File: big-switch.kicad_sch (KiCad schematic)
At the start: 7 parts, among them J1 Conn_01x07_Socket, SW1 SW_Push, SW2 RotaryEncoder_Switch, SW3 RotaryEncoder_Switch, U1 ProMicro

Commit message: routing ocmplete
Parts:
- J1: symbol Connector:Conn_01x07_Socket -> Connector:Conn_01x08_Socket
- SW2, SW3: footprint (none) -> Keebio-Parts:RotaryEncoder_EC11B-Horizontal-Dual
- U1: value ProMicro -> LonganNano; symbol keebio:ProMicro -> ws2812b:Longan_Nano
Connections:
- net VCC is gone; now on net +3V3: J1.2 (Pin_2)
- net +3V3: now also U1.2 (3.3v)
- net +5V: now also U1.1 (5v)
- net AUDIO: now also U1.24 (A2)
- net DISP_BL: now also J1.8 (Pin_8), U1.20 (C14); no longer J1.7 (Pin_7)
- net DISP_CS: now also J1.7 (Pin_7), U1.21 (C13); no longer J1.6 (Pin_6)
- net DISP_DC: now also J1.6 (Pin_6), U1.22 (A0); no longer J1.5 (Pin_5)
- net ENC1_A: now also U1.5 (B14)
- net ENC1_B: now also U1.6 (B15)
- net ENC1_SW: now also U1.7 (A8)
- net ENC2_A: now also U1.8 (A11)
- net ENC2_B: now also U1.9 (A12)
- net ENC2_SW: now also U1.10 (B4)
- net GND: now also U1.16 (GND), U1.17 (GND)
- net GPIO_X1: now also U1.31 (B1)
- net GPIO_X2: now also U1.30 (B0)
- net MISO: now also U1.28 (A6)
- net MOSI: now also U1.29 (A7)
- net SCL: now also U1.12 (B6)
- net SCLK: now also U1.27 (A5)
- net SDA: now also U1.13 (B7)
- net SW_1: now also U1.3 (B12)
- net VIK_CS: now also U1.26 (A4)
- net VIK_RGB: now also U1.32 (B10)
- no-connect marks 0 -> 9

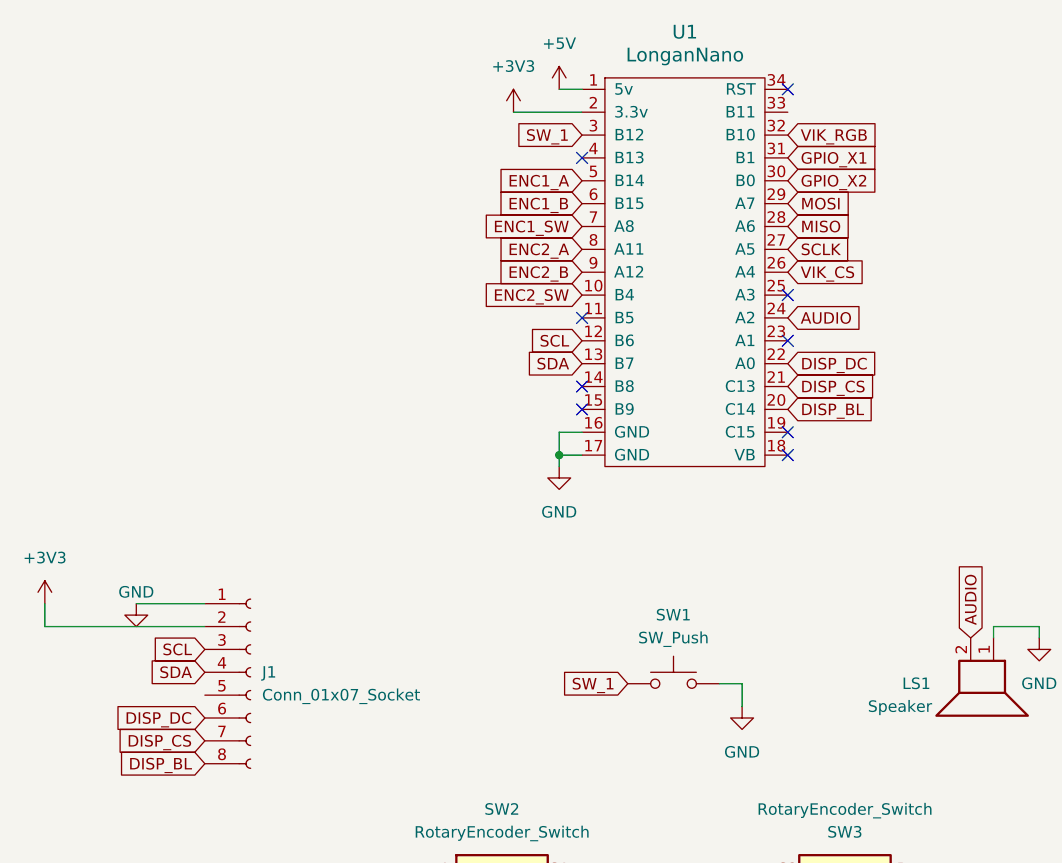
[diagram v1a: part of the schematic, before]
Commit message: flipped mcu side, rerouted
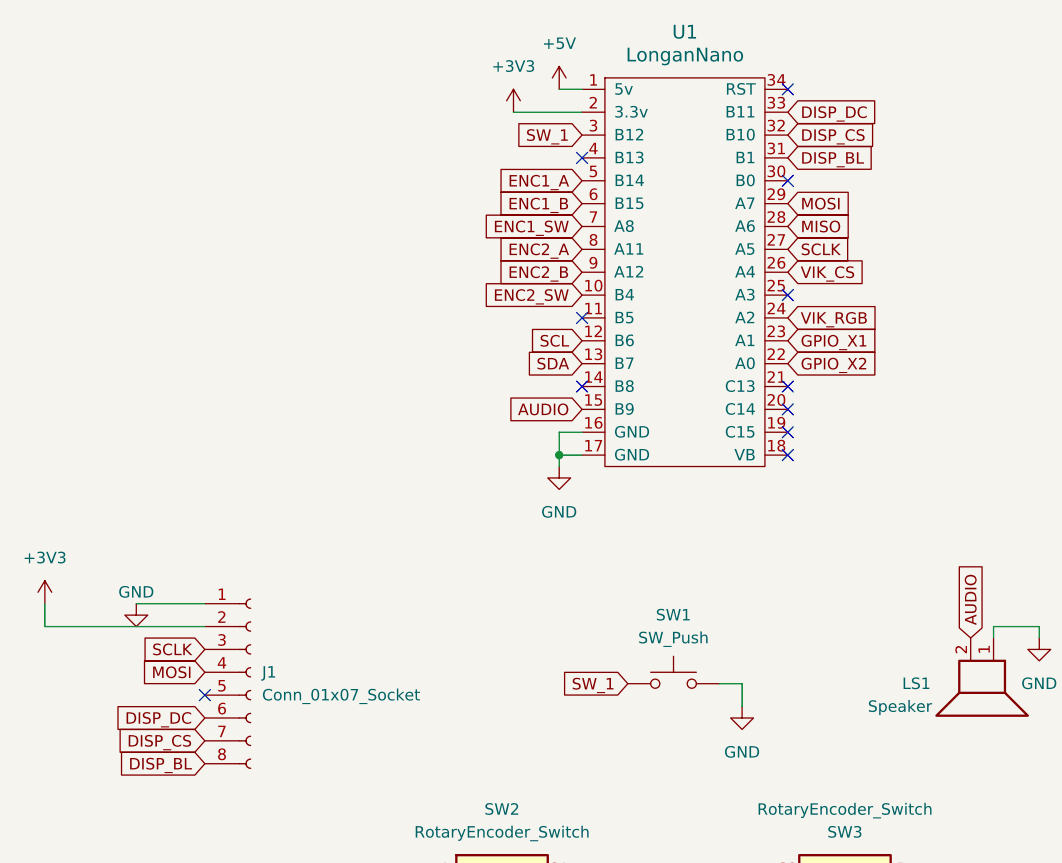
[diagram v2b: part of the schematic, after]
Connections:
- net AUDIO: now also U1.15 (B9); no longer U1.24 (A2)
- net DISP_BL: now also U1.31 (B1); no longer U1.20 (C14)
- net DISP_CS: now also U1.32 (B10); no longer U1.21 (C13)
- net DISP_DC: now also U1.33 (B11); no longer U1.22 (A0)
- net GPIO_X1: now also U1.23 (A1); no longer U1.31 (B1)
- net GPIO_X2: now also U1.22 (A0); no longer U1.30 (B0)
- net MOSI: now also J1.4 (Pin_4)
- net SCL: no longer J1.3 (Pin_3)
- net SCLK: now also J1.3 (Pin_3)
- net SDA: no longer J1.4 (Pin_4)
- net VIK_RGB: now also U1.24 (A2); no longer U1.32 (B10)
- no-connect marks 9 -> 11

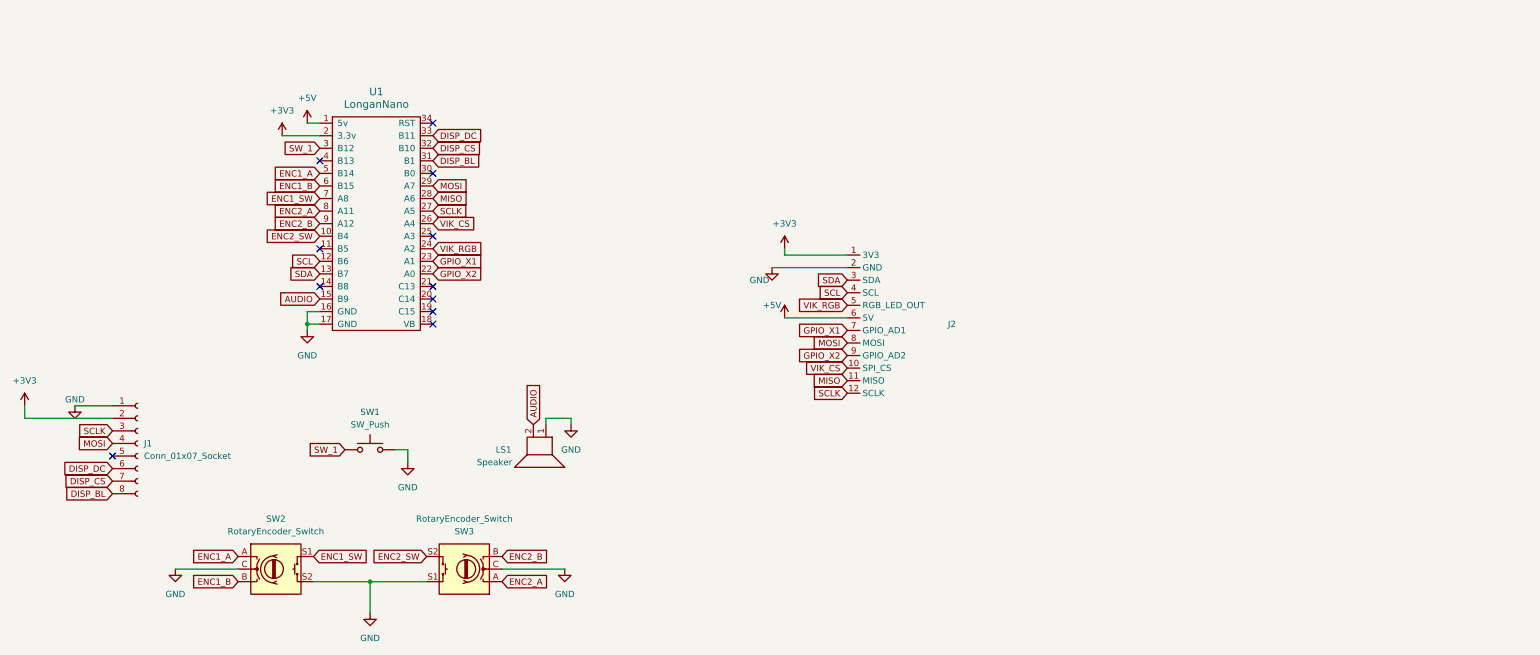
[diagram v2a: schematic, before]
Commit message: added LED
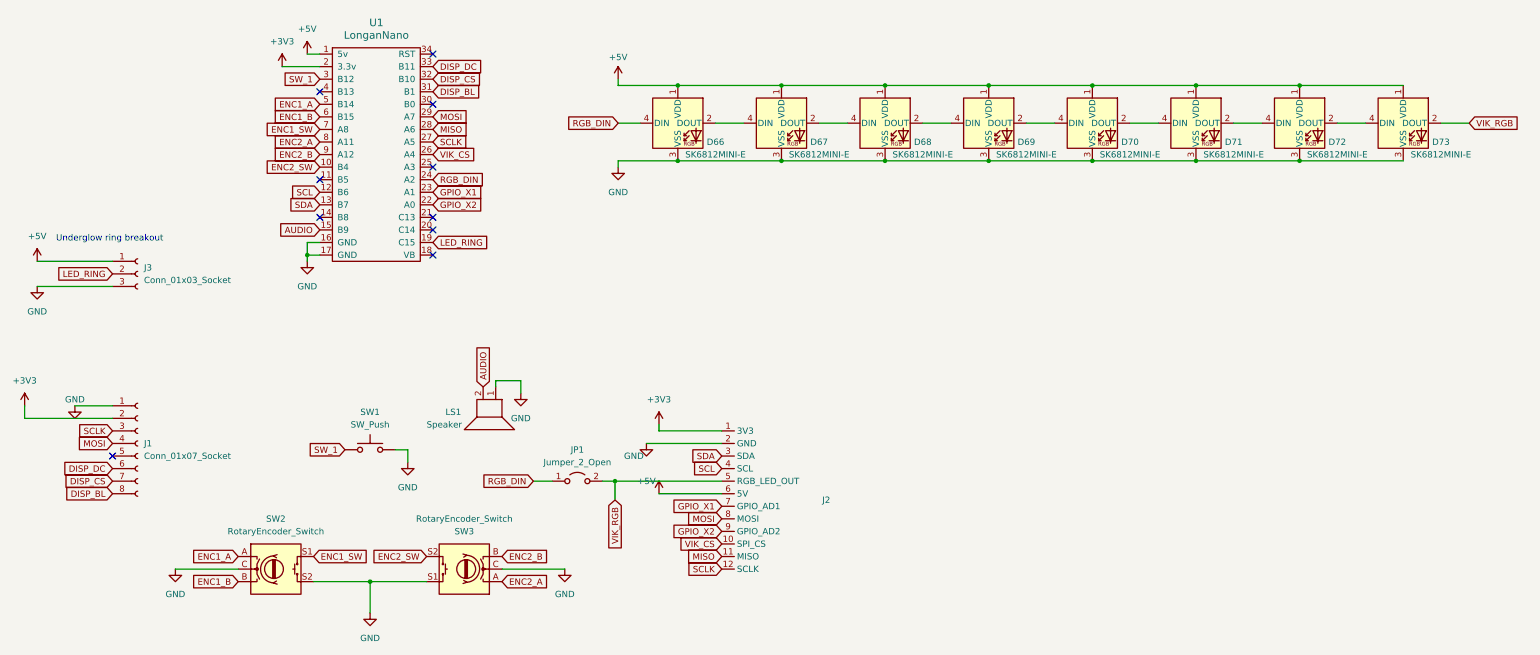
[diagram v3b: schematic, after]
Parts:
- added D66, D67, D68, D69, D70, D71, D72, D73: SK6812MINI-E, Keebio-Parts:SK6812-MINI-E, symbol 0xcb:SK6812MINI-E
- added J3: Conn_01x03_Socket, Connector_PinHeader_2.54mm:PinHeader_1x03_P2.54mm_Vertical, symbol Connector:Conn_01x03_Socket
- added JP1: Jumper_2_Open, Jumper:SolderJumper-2_P1.3mm_Open_RoundedPad1.0x1.5mm, symbol Jumper:Jumper_2_Open
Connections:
- net +5V: now also D66.1 (VDD), D67.1 (VDD), D68.1 (VDD), D69.1 (VDD), D70.1 (VDD), D71.1 (VDD), D72.1 (VDD), D73.1 (VDD), J3.1 (Pin_1)
- net GND: now also D66.3 (VSS), D67.3 (VSS), D68.3 (VSS), D69.3 (VSS), D70.3 (VSS), D71.3 (VSS), D72.3 (VSS), D73.3 (VSS), J3.3 (Pin_3)
- net VIK_RGB: now also D73.2 (DOUT), JP1.2 (B); no longer U1.24 (A2)
- net LED_RING: now reaches U1.19 (C15)
- net LED_RING: now also J3.2 (Pin_2)
- new net: D69.2 (DOUT), D70.4 (DIN)
- new net: D68.2 (DOUT), D69.4 (DIN)
- new net: D70.2 (DOUT), D71.4 (DIN)
- new net: D71.2 (DOUT), D72.4 (DIN)
- new net: D67.2 (DOUT), D68.4 (DIN)
- new net: D66.2 (DOUT), D67.4 (DIN)
- new net: D72.2 (DOUT), D73.4 (DIN)
- new net RGB_DIN: D66.4 (DIN), JP1.1 (A), U1.24 (A2)
- no-connect marks 11 -> 10
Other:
- note added: "Underglow ring breakout"
- moved on the sheet: J2, LS1, U1

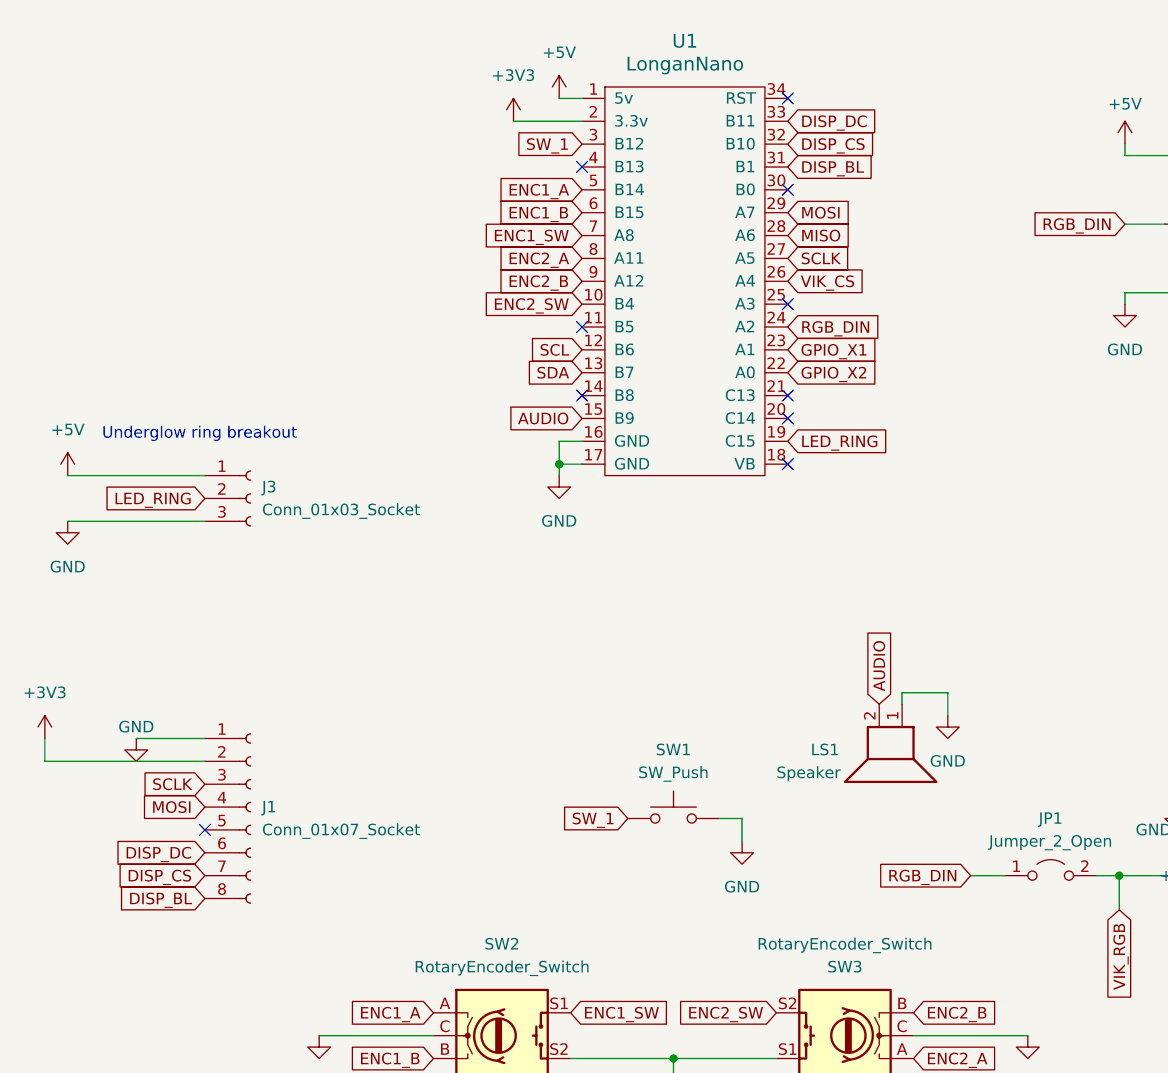
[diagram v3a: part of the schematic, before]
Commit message: updted to support rp2040-zero
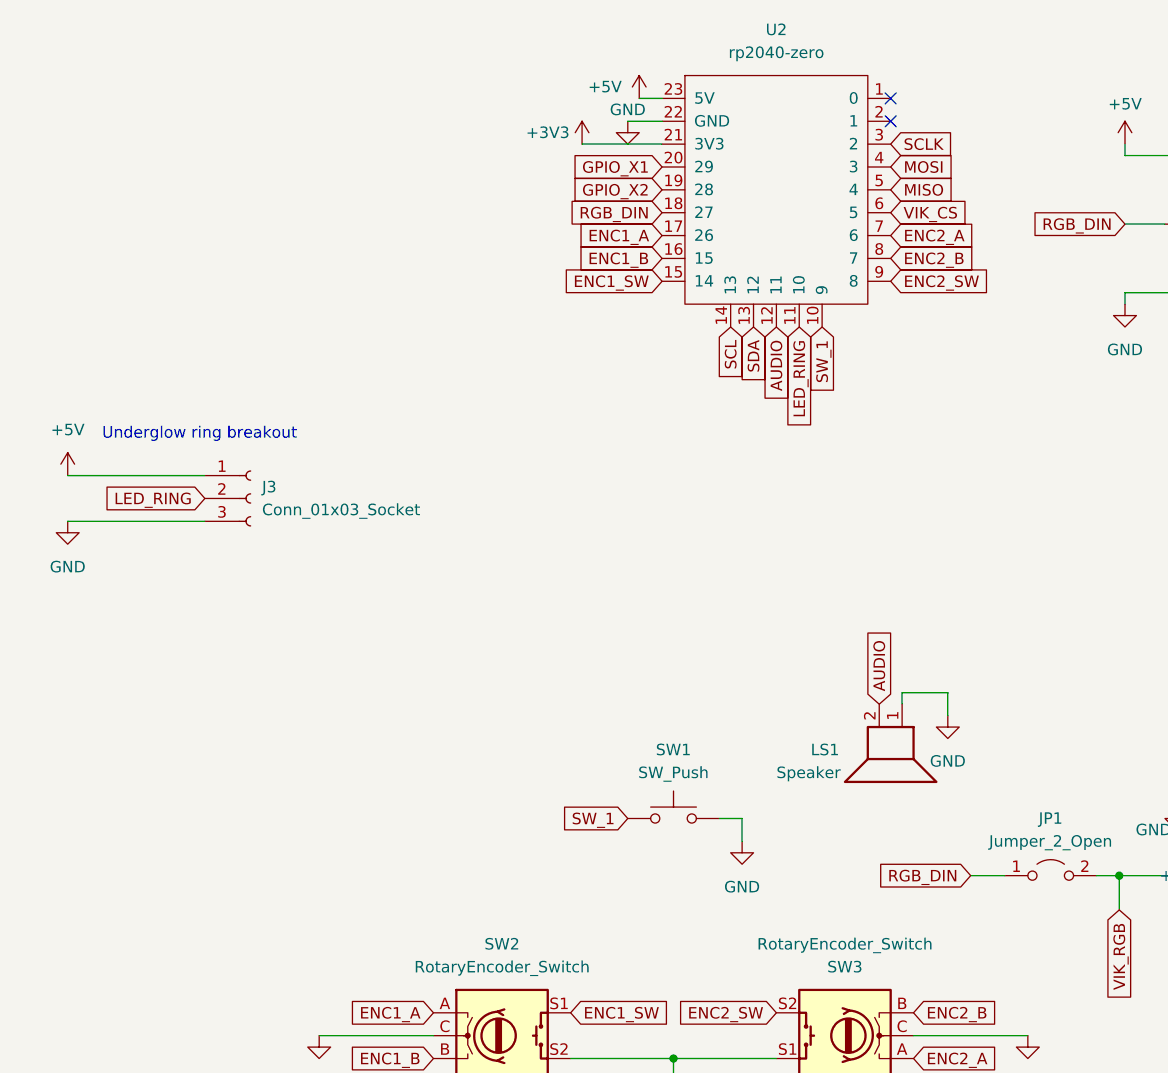
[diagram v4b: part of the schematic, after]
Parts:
- removed J1: Conn_01x07_Socket, Connector_PinHeader_2.54mm:PinHeader_1x07_P2.54mm_Horizontal, symbol Connector:Conn_01x08_Socket
- removed U1: LonganNano, prsid:Longan_Nano, symbol ws2812b:Longan_Nano
- added U2: rp2040-zero, prsid:rp2040-zero-tht, symbol mcu:rp2040-zero
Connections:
- net +3V3: now also U2.21 (3V3)
- net +5V: now also U2.23 (5V)
- net AUDIO: now also U2.12 (11)
- net ENC1_A: now also U2.17 (26)
- net ENC1_B: now also U2.16 (15)
- net ENC1_SW: now also U2.15 (14)
- net ENC2_A: now also U2.7 (6)
- net ENC2_B: now also U2.8 (7)
- net ENC2_SW: now also U2.9 (8)
- net GND: now also U2.22 (GND)
- net GPIO_X1: now also U2.20 (29)
- net GPIO_X2: now also U2.19 (28)
- net LED_RING: now also U2.11 (10)
- net MISO: now also U2.5 (4)
- net MOSI: now also U2.4 (3)
- net RGB_DIN: now also U2.18 (27)
- net SCL: now also U2.14 (13)
- net SCLK: now also U2.3 (2)
- net SDA: now also U2.13 (12)
- net SW_1: now also U2.10 (9)
- net VIK_CS: now also U2.6 (5)
- no-connect marks 10 -> 2
